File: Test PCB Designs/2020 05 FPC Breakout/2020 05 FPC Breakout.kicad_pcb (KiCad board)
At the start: 2 copper layers, 2 parts, among them J1 Conn_01x12_Female, J2 Conn_01x12_Female

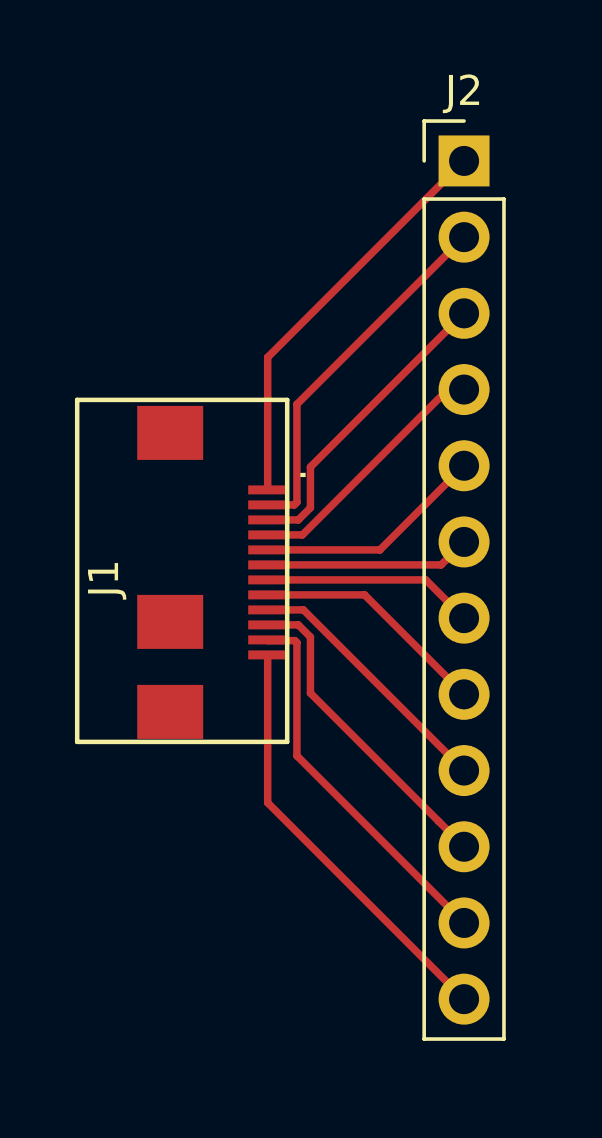
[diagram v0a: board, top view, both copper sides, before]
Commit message: FPC Breakout
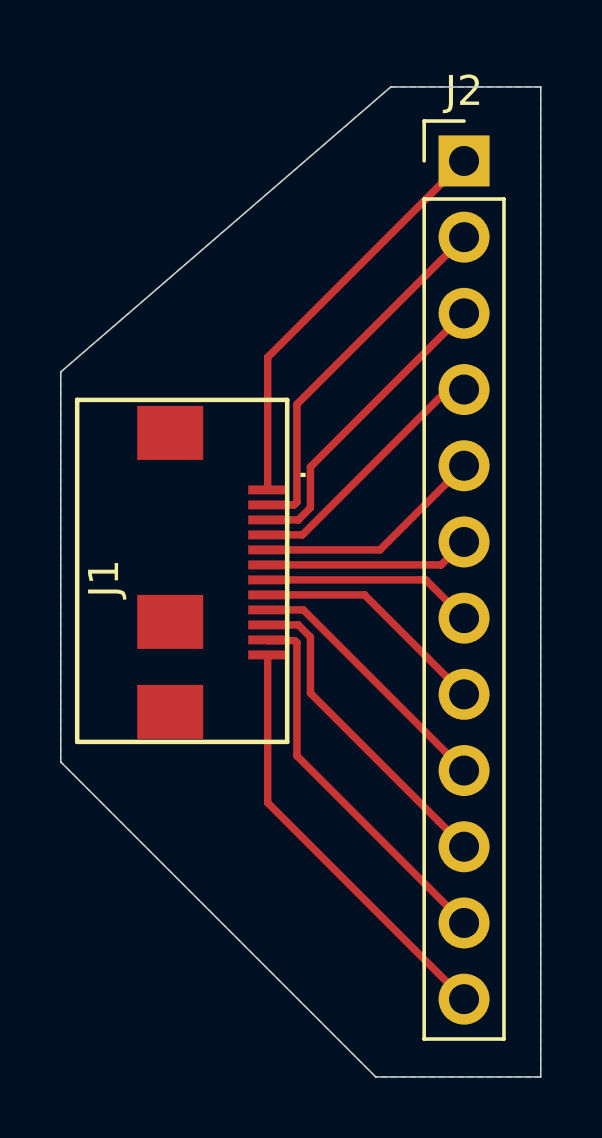
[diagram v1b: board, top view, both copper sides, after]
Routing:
- added copper zone on B.Cu, net (none)
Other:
- board outline added: 16 x 33 mm
- board text added: "BVH - AB4EN 6/12 0.5mm FPC sensor breakout"
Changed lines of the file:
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@@
-(kicad_pcb (version 20171130) (host pcbnew "(5.1.6-0-10_14)")
+(kicad_pcb (version 20171130) (host pcbnew 5.1.6-c6e7f7d~86~ubuntu18.04.1)
   (general
     (thickness 1.6)
-    (drawings 0)
+    (drawings 7)
     (tracks 35)
     (zones 0)
@@
       (outputformat 1)
       (mirror false)
-      (drillshape 1)
+      (drillshape 0)
       (scaleselection 1)
-      (outputdirectory ""))
+      (outputdirectory "order 2020-05-28/"))
   )
   (net 0 "")
@@
       (effects (font (size 1 1) (thickness 0.15)))
     )
+    (fp_line (start 1.8 -1.8) (end -1.8 -1.8) (layer F.CrtYd) (width 0.05))
+    (fp_line (start 1.8 29.75) (end 1.8 -1.8) (layer F.CrtYd) (width 0.05))
+    (fp_line (start -1.8 29.75) (end 1.8 29.75) (layer F.CrtYd) (width 0.05))
+    (fp_line (start -1.8 -1.8) (end -1.8 29.75) (layer F.CrtYd) (width 0.05))
+    (fp_line (start -1.33 -1.33) (end 0 -1.33) (layer F.SilkS) (width 0.12))
+    (fp_line (start -1.33 0) (end -1.33 -1.33) (layer F.SilkS) (width 0.12))
+    (fp_line (start -1.33 1.27) (end 1.33 1.27) (layer F.SilkS) (width 0.12))
+    (fp_line (start 1.33 1.27) (end 1.33 29.27) (layer F.SilkS) (width 0.12))
+    (fp_line (start -1.33 1.27) (end -1.33 29.27) (layer F.SilkS) (width 0.12))
+    (fp_line (start -1.33 29.27) (end 1.33 29.27) (layer F.SilkS) (width 0.12))
+    (fp_line (start -1.27 -0.635) (end -0.635 -1.27) (layer F.Fab) (width 0.1))
+    (fp_line (start -1.27 29.21) (end -1.27 -0.635) (layer F.Fab) (width 0.1))
+    (fp_line (start 1.27 29.21) (end -1.27 29.21) (layer F.Fab) (width 0.1))
+    (fp_line (start 1.27 -1.27) (end 1.27 29.21) (layer F.Fab) (width 0.1))
+    (fp_line (start -0.635 -1.27) (end 1.27 -1.27) (layer F.Fab) (width 0.1))
     (fp_text user %R (at 0 13.97 90) (layer F.Fab)
       (effects (font (size 1 1) (thickness 0.15)))
     )
-    (fp_line (start -0.635 -1.27) (end 1.27 -1.27) (layer F.Fab) (width 0.1))
-    (fp_line (start 1.27 -1.27) (end 1.27 29.21) (layer F.Fab) (width 0.1))
-    (fp_line (start 1.27 29.21) (end -1.27 29.21) (layer F.Fab) (width 0.1))
-    (fp_line (start -1.27 29.21) (end -1.27 -0.635) (layer F.Fab) (width 0.1))
-    (fp_line (start -1.27 -0.635) (end -0.635 -1.27) (layer F.Fab) (width 0.1))
-    (fp_line (start -1.33 29.27) (end 1.33 29.27) (layer F.SilkS) (width 0.12))
-    (fp_line (start -1.33 1.27) (end -1.33 29.27) (layer F.SilkS) (width 0.12))
-    (fp_line (start 1.33 1.27) (end 1.33 29.27) (layer F.SilkS) (width 0.12))
-    (fp_line (start -1.33 1.27) (end 1.33 1.27) (layer F.SilkS) (width 0.12))
-    (fp_line (start -1.33 0) (end -1.33 -1.33) (layer F.SilkS) (width 0.12))
-    (fp_line (start -1.33 -1.33) (end 0 -1.33) (layer F.SilkS) (width 0.12))
-    (fp_line (start -1.8 -1.8) (end -1.8 29.75) (layer F.CrtYd) (width 0.05))
-    (fp_line (start -1.8 29.75) (end 1.8 29.75) (layer F.CrtYd) (width 0.05))
-    (fp_line (start 1.8 29.75) (end 1.8 -1.8) (layer F.CrtYd) (width 0.05))
-    (fp_line (start 1.8 -1.8) (end -1.8 -1.8) (layer F.CrtYd) (width 0.05))
     (pad 12 thru_hole oval (at 0 27.94) (size 1.7 1.7) (drill 1) (layers *.Cu *.Mask)
       (net 1 "Net-(J1-Pad12)"))
@@
       (effects (font (size 1 1) (thickness 0.15)))
     )
+    (fp_line (start -3 6.35) (end -3 -0.65) (layer F.SilkS) (width 0.15))
+    (fp_line (start 8.4 6.35) (end -3 6.35) (layer F.SilkS) (width 0.15))
+    (fp_line (start 8.4 -0.65) (end 8.4 6.35) (layer F.SilkS) (width 0.15))
+    (fp_line (start -3 -0.65) (end 8.4 -0.65) (layer F.SilkS) (width 0.15))
     (fp_text user . (at -0.5 -0.8 90) (layer F.SilkS)
       (effects (font (size 1 1) (thickness 0.15)))
     )
-    (fp_line (start -3 -0.65) (end 8.4 -0.65) (layer F.SilkS) (width 0.15))
-    (fp_line (start 8.4 -0.65) (end 8.4 6.35) (layer F.SilkS) (width 0.15))
-    (fp_line (start 8.4 6.35) (end -3 6.35) (layer F.SilkS) (width 0.15))
-    (fp_line (start -3 6.35) (end -3 -0.65) (layer F.SilkS) (width 0.15))
     (pad "" smd rect (at 4.4 3.25 270) (size 1.8 2.2) (layers F.Cu F.Paste F.Mask))
     (pad 12 smd rect (at 5.5 0 270) (size 0.3 1.3) (layers F.Cu F.Paste F.Mask)
@@
     (pad "" smd rect (at 7.4 3.25 270) (size 1.8 2.2) (layers F.Cu F.Paste F.Mask))
   )
+  (gr_text "BVH - AB4EN\n6/12 0.5mm FPC sensor breakout" (at 137.5 90 90) (layer B.SilkS)
+    (effects (font (size 1 1) (thickness 0.15)) (justify mirror))
+  )
+  (gr_line (start 140.5 73.5) (end 145.5 73.5) (layer Edge.Cuts) (width 0.05))
+  (gr_line (start 129.5 83) (end 140.5 73.5) (layer Edge.Cuts) (width 0.05))
+  (gr_line (start 129.5 96) (end 129.5 83) (layer Edge.Cuts) (width 0.05))
+  (gr_line (start 140 106.5) (end 129.5 96) (layer Edge.Cuts) (width 0.05))
+  (gr_line (start 145.5 106.5) (end 140 106.5) (layer Edge.Cuts) (width 0.05))
+  (gr_line (start 145.5 73.5) (end 145.5 106.5) (layer Edge.Cuts) (width 0.05))
   (segment (start 136.398 97.3605) (end 142.944 103.9065) (width 0.25) (layer F.Cu) (net 1))
   (segment (start 136.398 92.4315) (end 136.398 97.3605) (width 0.25) (layer F.Cu) (net 1))
@@
   (segment (start 142.179 89.4315) (end 142.944 88.6665) (width 0.25) (layer F.Cu) (net 12))
   (segment (start 136.398 89.4315) (end 142.179 89.4315) (width 0.25) (layer F.Cu) (net 12))
+  (zone (net 0) (net_name "") (layer B.Cu) (hatch edge 0.508)
+    (connect_pads (clearance 0.508))
+    (min_thickness 0.254)
+    (fill yes (arc_segments 32) (thermal_gap 0.508) (thermal_bridge_width 0.508))
+    (polygon
+      (pts
+        (xy 145.5 106.5) (xy 140 106.5) (xy 129.5 96) (xy 129.5 83) (xy 140.5 73.5)
+        (xy 145.5 73.5)
+      )
+    )
+  )
 )
